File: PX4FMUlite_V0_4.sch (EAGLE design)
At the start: 132 parts, among them J2 DF13-4P-1.25V, J201 DF13C-6P-1.25V, J202 DF13C-6P-1.25V, J203 DF13C-6P-1.25V, J3 DF13C-4P-1.25V, J302 DF13C-4P-1.25V, J401 DF13C-4P-1.25V, J403 DF13C-7P-1.25V, J405 DF13C-4P-1.25V, J802 DF13C-3P-1.25V, M3_MOUNT1101 MOUNT-HOLE3.1MM, M3_MOUNT1102 MOUNT-HOLE3.1MM, M3_MOUNT1103 MOUNT-HOLE3.1MM, M3_MOUNT1104 MOUNT-HOLE3.1MM, U101 STM32F4X7VX, U2 MAX3051, U401 MAX3051, X101 3.2x2.5 mm / 24 MHz / 15 ppm

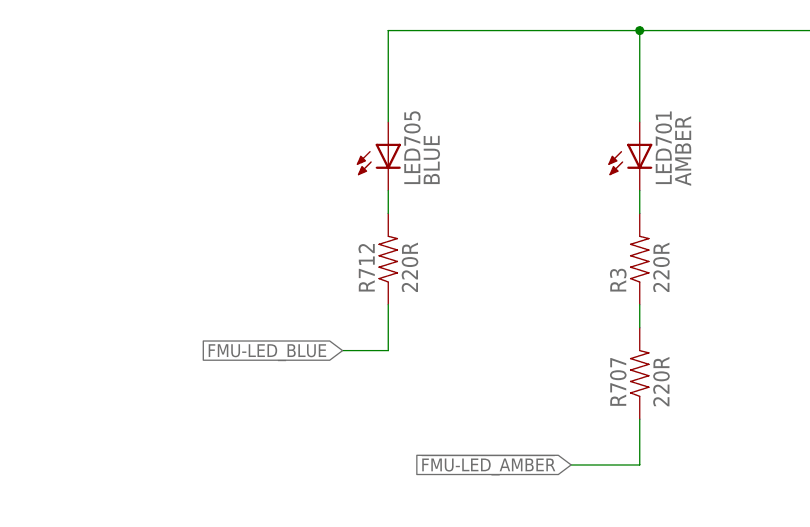
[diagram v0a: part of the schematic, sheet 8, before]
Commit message: Blue LED removed
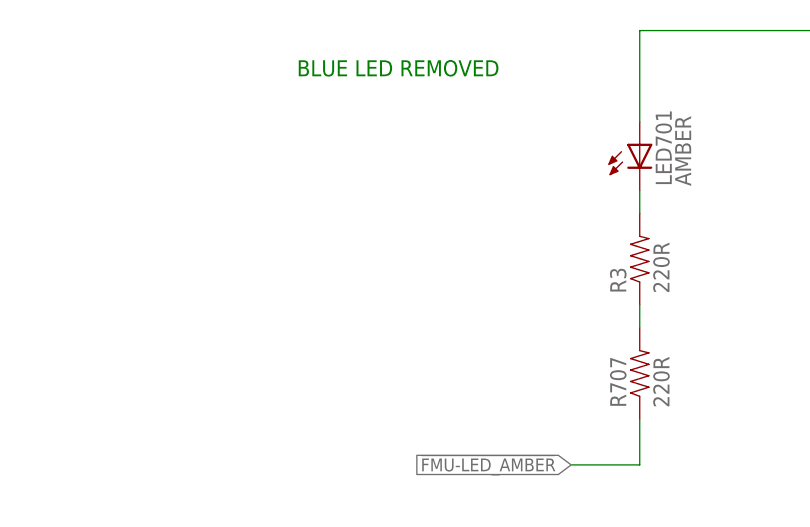
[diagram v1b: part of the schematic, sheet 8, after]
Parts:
- removed LED705: BLUE, pixhawk2:LED0603
- removed R712: 220R, pixhawk2:RESISTOR0402-RES
- removed U$402: PESD0402-140, pixhawk2:DIODE-TVS
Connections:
- removed net FMU-LED_BLUE: R712.1
- removed net N$9: LED705.C, R712.2
- net GND: no longer U$402.A
- net N$41: no longer U$402.C
- net VDD_5V: no longer LED705.A
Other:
- note added: "BLUE LED REMOVED"
- note added: "ESD PROTECTOR REMOVED"
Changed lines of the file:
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@@
 <attribute name="PARTNO" value="C1608Y5V1C225Z"/>
 </part>
-<part name="LED705" library="pixhawk2" deviceset="LED" device="0603" value="BLUE">
-<attribute name="PARTNO" value="APTD1608QBC/D"/>
-</part>
-<part name="R712" library="pixhawk2" deviceset="RESISTOR" device="0402-RES" value="220R">
-<attribute name="PARTNO" value="RC0402FR-07220RL"/>
-</part>
 <part name="C505" library="pixhawk2" deviceset="CAP" device="0402" value="10n">
 <attribute name="PARTNO" value="CC0402KRX7R7BB103"/>
@@
 <attribute name="PARTNO" value="PESD0402-140"/>
 </part>
-<part name="U$402" library="pixhawk2" deviceset="DIODE-TVS" device="" value="PESD0402-140">
-<attribute name="PARTNO" value="PESD0402-140"/>
-</part>
 <part name="U$404" library="pixhawk2" deviceset="DIODE-TVS" device="" value="PESD0402-140">
 <attribute name="PARTNO" value="PESD0402-140"/>
@@
 <text x="22.86" y="170.18" size="1.778" layer="91">Note: SPI port is UNBUFFERED; only suitable for short connections.</text>
 <text x="93.98" y="83.82" size="1.778" layer="97">I2C1</text>
+<text x="83.82" y="162.56" size="1.778" layer="91">ESD PROTECTOR REMOVED</text>
 </plain>
 <instances>
@@
 <attribute name="PARTNO" x="182.88" y="66.04" size="1.778" layer="96" display="off"/>
 </instance>
-<instance part="U$402" gate="G$1" x="81.28" y="157.48" rot="R90">
-<attribute name="PARTNO" x="81.28" y="157.48" size="1.778" layer="96" display="off"/>
-</instance>
 <instance part="U$404" gate="G$1" x="226.06" y="58.42" rot="R90">
 <attribute name="PARTNO" x="226.06" y="58.42" size="1.778" layer="96" display="off"/>
@@
 <wire x1="88.9" y1="154.94" x2="86.36" y2="154.94" width="0.1524" layer="91"/>
 <wire x1="86.36" y1="154.94" x2="86.36" y2="160.02" width="0.1524" layer="91"/>
-<wire x1="86.36" y1="160.02" x2="81.28" y2="160.02" width="0.1524" layer="91"/>
 <pinref part="L402" gate="G$1" pin="P$2"/>
-<pinref part="U$402" gate="G$1" pin="C"/>
-<wire x1="81.28" y1="160.02" x2="66.04" y2="160.02" width="0.1524" layer="91"/>
-<junction x="81.28" y="160.02"/>
+<wire x1="86.36" y1="160.02" x2="66.04" y2="160.02" width="0.1524" layer="91"/>
 </segment>
 </net>
@@
 <wire x1="60.96" y1="139.7" x2="60.96" y2="154.94" width="0.1524" layer="91"/>
 <junction x="88.9" y="139.7"/>
-<pinref part="U$402" gate="G$1" pin="A"/>
 <wire x1="81.28" y1="154.94" x2="81.28" y2="139.7" width="0.1524" layer="91"/>
 <junction x="81.28" y="139.7"/>
@@
 Selected R: 220
 Cacluated If @ 5.5V: 10mA</text>
+<text x="142.24" y="149.86" size="1.778" layer="91">BLUE LED REMOVED</text>
 </plain>
 <instances>
@@
 </instance>
 <instance part="GND14" gate="1" x="203.2" y="121.92"/>
-<instance part="LED705" gate="G$1" x="152.4" y="142.24">
-<attribute name="PARTNO" x="152.4" y="142.24" size="1.778" layer="96" display="off"/>
-</instance>
-<instance part="R712" gate="G$1" x="152.4" y="129.54" rot="R90">
-<attribute name="PARTNO" x="152.4" y="129.54" size="1.778" layer="96" display="off"/>
-</instance>
 <instance part="R713" gate="G$1" x="121.92" y="50.8" smashed="yes" rot="R270">
 <attribute name="NAME" x="118.3386" y="52.07" size="1.778" layer="95" rot="R270"/>
@@
 </segment>
 </net>
-<net name="N$9" class="0">
-<segment>
-<wire x1="152.4" y1="137.16" x2="152.4" y2="134.62" width="0.1524" layer="91"/>
-<pinref part="LED705" gate="G$1" pin="C"/>
-<pinref part="R712" gate="G$1" pin="2"/>
-</segment>
-</net>
-<net name="FMU-LED_BLUE" class="0">
-<segment>
-<wire x1="152.4" y1="119.38" x2="147.32" y2="119.38" width="0.1524" layer="91"/>
-<wire x1="152.4" y1="124.46" x2="152.4" y2="119.38" width="0.1524" layer="91"/>
-<label x="147.32" y="119.38" size="1.4224" layer="95" rot="R180" xref="yes"/>
-<pinref part="R712" gate="G$1" pin="1"/>
-</segment>
-</net>
 <net name="SAFETY" class="0">
 <segment>
@@
 <wire x1="203.2" y1="154.94" x2="210.82" y2="154.94" width="0.1524" layer="91"/>
 <junction x="203.2" y="154.94"/>
-<pinref part="LED705" gate="G$1" pin="A"/>
-<wire x1="152.4" y1="144.78" x2="152.4" y2="154.94" width="0.1524" layer="91"/>
-<wire x1="152.4" y1="154.94" x2="180.34" y2="154.94" width="0.1524" layer="91"/>
-<junction x="180.34" y="154.94"/>
 </segment>
 </net>
@@
 </segment>
 </net>
-<net name="VDD_3V3_SPEKTRUM" class="1">
-<segment>
-<label x="104.14" y="71.12" size="1.27" layer="95" rot="R180" xref="yes"/>
-<wire x1="104.14" y1="71.12" x2="121.92" y2="71.12" width="0.1524" layer="91"/>
-<wire x1="121.92" y1="71.12" x2="121.92" y2="55.88" width="0.1524" layer="91"/>
-<wire x1="121.92" y1="55.88" x2="127" y2="55.88" width="0.1524" layer="91"/>
-</segment>
-</net>

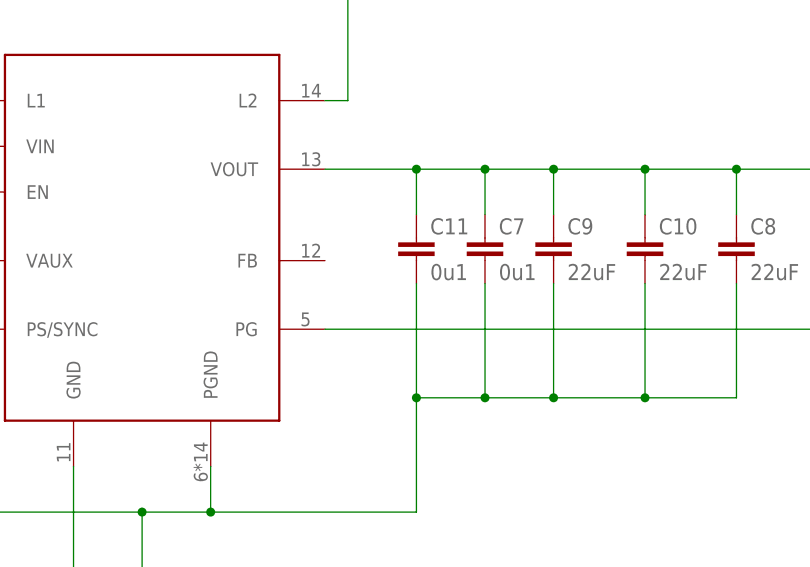
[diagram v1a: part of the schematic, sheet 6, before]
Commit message: Positioned buckboost Vaux decoupling cap
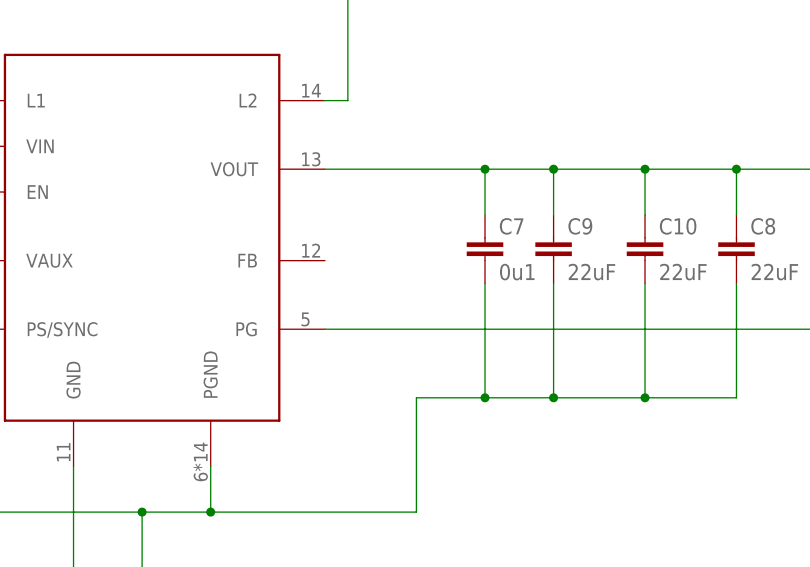
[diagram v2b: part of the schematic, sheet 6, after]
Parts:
- removed C11: 0u1, pixhawk2:CAP0402
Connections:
- net GND: no longer C11.2
- net VDD_5V: no longer C11.1
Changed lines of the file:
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@@
-<attribute name="PARTNO" value="CC0402ZRY5V7BB104"/>
-</part>
-<part name="C11" library="pixhawk2" deviceset="CAP" device="0402" value="0u1">
 <attribute name="PARTNO" value="CC0402ZRY5V7BB104"/>
 </part>
@@
 <attribute name="PARTNO" x="139.7" y="111.76" size="1.778" layer="96" display="off"/>
 </instance>
-<instance part="C11" gate="G$1" x="132.08" y="111.76">
-<attribute name="PARTNO" x="132.08" y="111.76" size="1.778" layer="96" display="off"/>
-</instance>
 <instance part="C12" gate="G$1" x="60.96" y="104.14">
 <attribute name="PARTNO" x="60.96" y="104.14" size="1.778" layer="96" display="off"/>
@@
 <wire x1="68.58" y1="73.66" x2="76.2" y2="73.66" width="0.1524" layer="91"/>
 <junction x="76.2" y="73.66"/>
-<wire x1="132.08" y1="109.22" x2="132.08" y2="96.52" width="0.1524" layer="91"/>
 <pinref part="C7" gate="G$1" pin="2"/>
 <wire x1="139.7" y1="109.22" x2="139.7" y2="96.52" width="0.1524" layer="91"/>
 <junction x="139.7" y="96.52"/>
-<junction x="132.08" y="96.52"/>
-<pinref part="C11" gate="G$1" pin="2"/>
 <pinref part="C12" gate="G$1" pin="2"/>
 <wire x1="60.96" y1="101.6" x2="60.96" y2="83.82" width="0.1524" layer="91"/>
@@
 <pinref part="U$15" gate="A" pin="VOUT"/>
 <pinref part="C8" gate="G$1" pin="1"/>
-<wire x1="121.92" y1="121.92" x2="132.08" y2="121.92" width="0.1524" layer="91"/>
-<wire x1="132.08" y1="121.92" x2="139.7" y2="121.92" width="0.1524" layer="91"/>
+<wire x1="121.92" y1="121.92" x2="139.7" y2="121.92" width="0.1524" layer="91"/>
 <wire x1="139.7" y1="121.92" x2="147.32" y2="121.92" width="0.1524" layer="91"/>
 <wire x1="147.32" y1="121.92" x2="157.48" y2="121.92" width="0.1524" layer="91"/>
@@
 <pinref part="C7" gate="G$1" pin="1"/>
 <wire x1="139.7" y1="116.84" x2="139.7" y2="121.92" width="0.1524" layer="91"/>
-<wire x1="132.08" y1="116.84" x2="132.08" y2="121.92" width="0.1524" layer="91"/>
-<junction x="132.08" y="121.92"/>
 <junction x="139.7" y="121.92"/>
-<pinref part="C11" gate="G$1" pin="1"/>
-</segment>
-</net>
+</segment>
+</net>
